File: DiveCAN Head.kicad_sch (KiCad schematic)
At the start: 50 parts, among them J1 Cell 1, J10 SOLENOID OUT, J2 Cell 2, J3 Cell 3, J4 POWER CONNECTION, Q2 DMG1012T, U13 TPS63001, U15 74LVC2G14, U16 TPS63001

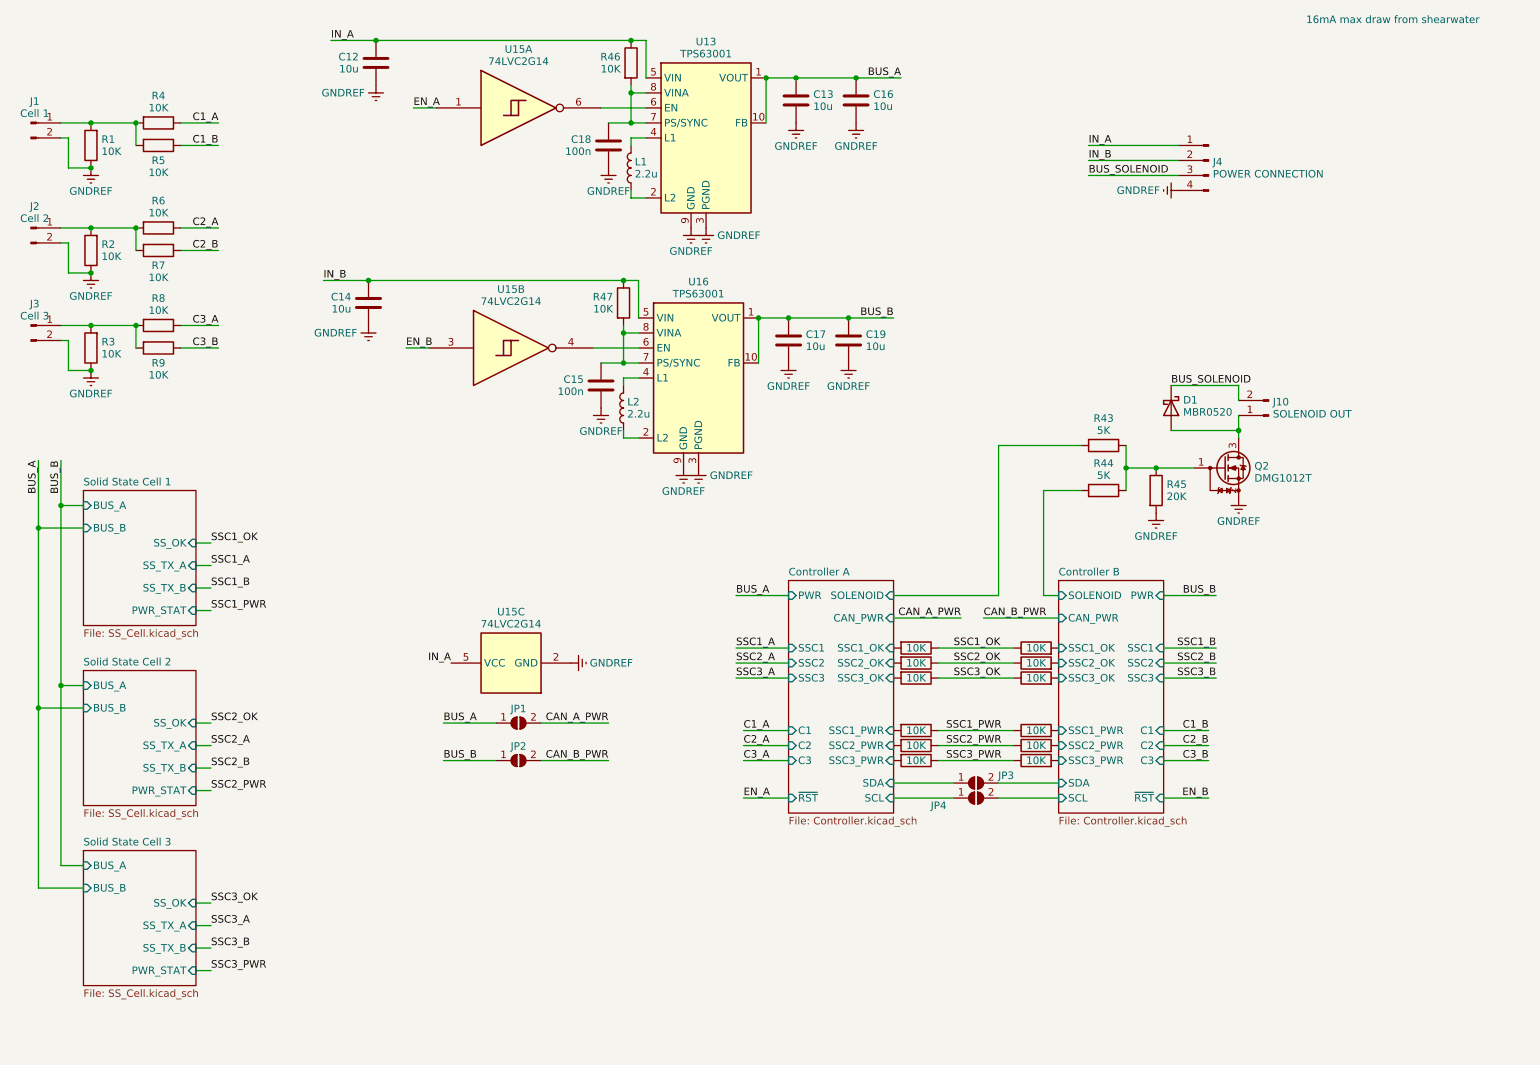
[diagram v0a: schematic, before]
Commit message: 
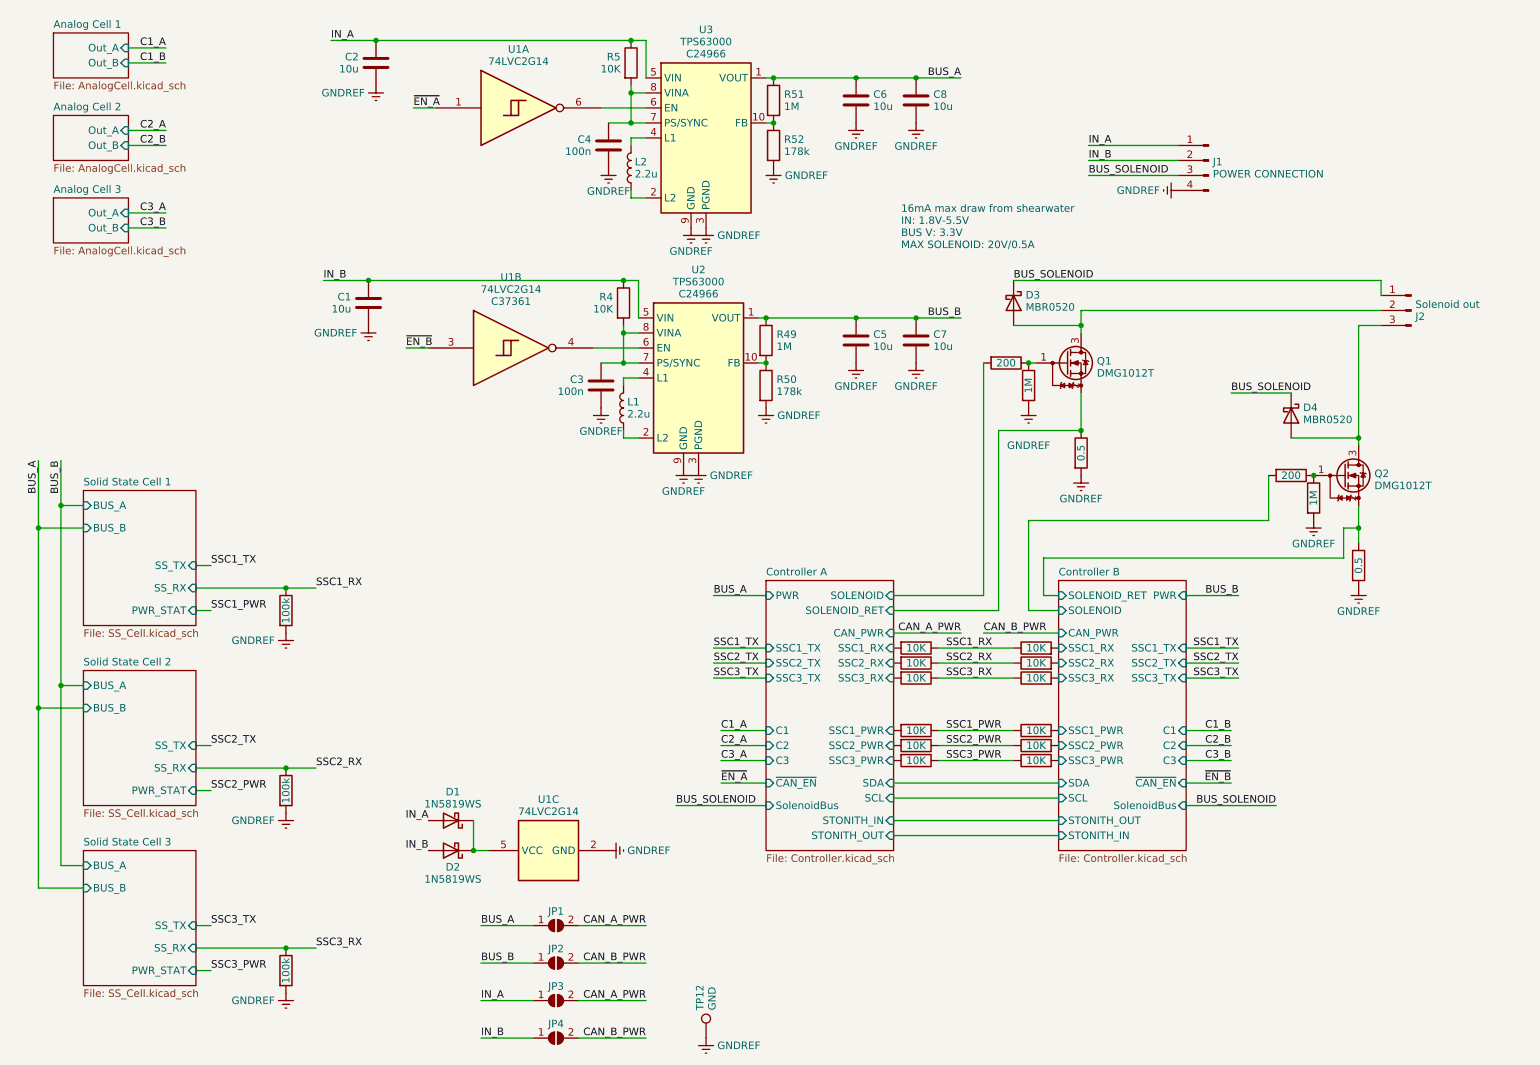
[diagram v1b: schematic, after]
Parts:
- removed J1: Cell 1, Connector_PinHeader_1.00mm:PinHeader_1x02_P1.00mm_Vertical, symbol Connector:Conn_01x02_Pin
- removed J10: SOLENOID OUT, Connector_PinHeader_1.00mm:PinHeader_1x02_P1.00mm_Vertical, symbol Connector:Conn_01x02_Pin
- removed J2: Cell 2, Connector_PinHeader_1.00mm:PinHeader_1x02_P1.00mm_Vertical, symbol Connector:Conn_01x02_Pin
- removed J3: Cell 3, Connector_PinHeader_1.00mm:PinHeader_1x02_P1.00mm_Vertical, symbol Connector:Conn_01x02_Pin
- removed R1, R2, R3, R4, R5, R6, R7, R8, R9: 10K, Resistor_SMD:R_0603_1608Metric, symbol Device:R
- removed R43, R44: 5K, Resistor_SMD:R_0603_1608Metric, symbol Device:R
- removed R45: 20K, Resistor_SMD:R_0603_1608Metric, symbol Device:R
- added D1, D2: 1N5819WS, Diode_SMD:D_SOD-323, symbol Device:D_Schottky
- added D3: MBR0520, Diode_SMD:D_SOD-123, symbol Diode:MBR0520
- added J2: Solenoid out, Connector_PinHeader_1.00mm:PinHeader_1x03_P1.00mm_Vertical, symbol Connector:Conn_01x03_Pin
- added Q1: DMG1012T, Package_TO_SOT_SMD:SOT-523, symbol Transistor_FET:DMG1012T
- added R1, R2, R3: 100k, Resistor_SMD:R_0402_1005Metric, symbol Project:R
- added R12, R21: 200, Resistor_SMD:R_0402_1005Metric, symbol Project:R
- added R13, R22, R49, R51: 1M, Resistor_SMD:R_0402_1005Metric, symbol Project:R
- added R20, R23: 0.5, Resistor_SMD:R_0402_1005Metric, symbol Project:R
- added R50, R52: 178k, Resistor_SMD:R_0402_1005Metric, symbol Project:R
- added TP12: GND, TestPoint:TestPoint_Pad_D1.0mm, symbol Connector:TestPoint
- C1: renamed from C14; MPN (none) -> C19702
- C2: renamed from C12; MPN (none) -> C19702
- C3: renamed from C15; MPN (none) -> C14663
- C4: renamed from C18; MPN (none) -> C14663
- C5: renamed from C17; MPN (none) -> C19702
- C6: renamed from C13; MPN (none) -> C19702
- C7: renamed from C19; MPN (none) -> C19702
- C8: renamed from C16; MPN (none) -> C19702
- D4: renamed from D1; MPN (none) -> C5204745
- J1: renamed from J4; now left out of the parts list
- L1: renamed from L2; footprint Inductor_SMD:L_Taiyo-Yuden_NR-30xx_HandSoldering -> Inductor_SMD:L_0805_2012Metric; MPN (none) -> C431245
- L2: renamed from L1; footprint Inductor_SMD:L_Taiyo-Yuden_NR-30xx_HandSoldering -> Inductor_SMD:L_0805_2012Metric; MPN (none) -> C431245
- Q2: JLCPCB Rotation Offset (none) -> 180; MPN (none) -> C20512
- R10: renamed from R14; footprint Resistor_SMD:R_0603_1608Metric -> Resistor_SMD:R_0402_1005Metric; symbol Device:R -> Project:R; MPN (none) -> C25744
- R11: renamed from R15; footprint Resistor_SMD:R_0603_1608Metric -> Resistor_SMD:R_0402_1005Metric; symbol Device:R -> Project:R; MPN (none) -> C25744
- R14: renamed from R16; footprint Resistor_SMD:R_0603_1608Metric -> Resistor_SMD:R_0402_1005Metric; symbol Device:R -> Project:R; MPN (none) -> C25744
- R15: renamed from R17; footprint Resistor_SMD:R_0603_1608Metric -> Resistor_SMD:R_0402_1005Metric; symbol Device:R -> Project:R; MPN (none) -> C25744
- R16: renamed from R18; footprint Resistor_SMD:R_0603_1608Metric -> Resistor_SMD:R_0402_1005Metric; symbol Device:R -> Project:R; MPN (none) -> C25744
- R17: renamed from R19; footprint Resistor_SMD:R_0603_1608Metric -> Resistor_SMD:R_0402_1005Metric; symbol Device:R -> Project:R; MPN (none) -> C25744
- R18: renamed from R20; footprint Resistor_SMD:R_0603_1608Metric -> Resistor_SMD:R_0402_1005Metric; symbol Device:R -> Project:R; MPN (none) -> C25744
- R19: renamed from R21; footprint Resistor_SMD:R_0603_1608Metric -> Resistor_SMD:R_0402_1005Metric; symbol Device:R -> Project:R; MPN (none) -> C25744
- R4: renamed from R47; footprint Resistor_SMD:R_0603_1608Metric -> Resistor_SMD:R_0402_1005Metric; symbol Device:R -> Project:R; MPN (none) -> C25744
- R5: renamed from R46; footprint Resistor_SMD:R_0603_1608Metric -> Resistor_SMD:R_0402_1005Metric; symbol Device:R -> Project:R; MPN (none) -> C25744
- R6: renamed from R10; footprint Resistor_SMD:R_0603_1608Metric -> Resistor_SMD:R_0402_1005Metric; symbol Device:R -> Project:R; MPN (none) -> C25744
- R7: renamed from R11; footprint Resistor_SMD:R_0603_1608Metric -> Resistor_SMD:R_0402_1005Metric; symbol Device:R -> Project:R; MPN (none) -> C25744
- R8: renamed from R12; footprint Resistor_SMD:R_0603_1608Metric -> Resistor_SMD:R_0402_1005Metric; symbol Device:R -> Project:R; MPN (none) -> C25744
- R9: renamed from R13; footprint Resistor_SMD:R_0603_1608Metric -> Resistor_SMD:R_0402_1005Metric; symbol Device:R -> Project:R; MPN (none) -> C25744
- U1: renamed from U15; footprint Package_SO:TSOP-6_1.65x3.05mm_P0.95mm -> Package_TO_SOT_SMD:SOT-363_SC-70-6; JLCPCB Rotation Offset (none) -> 180; MPN (none) -> C37361
- U1: renamed from U15; footprint Package_SO:TSOP-6_1.65x3.05mm_P0.95mm -> Package_TO_SOT_SMD:SOT-363_SC-70-6; symbol 74xGxx:74LVC2G14 -> Project:74LVC2G14; JLCPCB Rotation Offset (none) -> 180; MPN (none) -> C37361
- U2: renamed from U16; value TPS63001 -> TPS63000; footprint Package_SON:Texas_DRC0010J_ThermalVias -> Package_SON:Texas_DRC0010J; symbol Regulator_Switching:TPS63001 -> Project:TPS63001; MPN (none) -> C24966
- U3: renamed from U13; value TPS63001 -> TPS63000; footprint Package_SON:Texas_DRC0010J_ThermalVias -> Package_SON:Texas_DRC0010J; symbol Regulator_Switching:TPS63001 -> Project:TPS63001; MPN (none) -> C24966
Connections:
- net Controller B/SCL is gone; now on net CAN_B_PWR: JP4.2 (B)
- net Controller B/SDA is gone; now on net CAN_A_PWR: JP3.2 (B)
- net BUS_A: now also R51.1; no longer U3.10 (FB)
- net BUS_B: now also R49.1; no longer U2.10 (FB)
- net BUS_SOLENOID: now also D3.1 (K), J2.1 (Pin_1)
- net Controller A/SCL: no longer JP4.1 (A)
- net Controller A/SDA: no longer JP3.1 (A)
- net Controller A/SOLENOID: now also R12.2
- net Controller B/SOLENOID: now also R21.2
- net GNDREF: now also R1.2, R13.2, R2.2, R20.2, R22.2, R23.2, R3.2, R50.2, R52.2, TP12.1; no longer Q2.2 (S)
- net IN_A: now also JP3.1 (A), D1.2 (A); no longer U1.5 (VCC)
- net IN_B: now also JP4.1 (A), D2.2 (A)
- net at Q2.1 (G): now also R21.1, R22.1
- net at D4.2 (A), Q2.3 (D): now also J2.3 (Pin_3)
- net Controller A/SSC1_OK renamed Controller A/SSC1_RX
- net Controller A/SSC2_OK renamed Controller A/SSC2_RX
- net Controller A/SSC3_OK renamed Controller A/SSC3_RX
- net Controller B/SSC1_OK renamed Controller B/SSC1_RX
- net Controller B/SSC2_OK renamed Controller B/SSC2_RX
- net Controller B/SSC3_OK renamed Controller B/SSC3_RX
- net EN_A renamed ~{EN_A}
- net EN_B renamed ~{EN_B}
- net SSC1_OK renamed SSC1_RX
- net SSC1_RX: now also R1.1
- net SSC2_OK renamed SSC2_RX
- net SSC2_RX: now also R2.1
- net SSC3_OK renamed SSC3_RX
- net SSC3_RX: now also R3.1
- new net: D3.2 (A), J2.2 (Pin_2), Q1.3 (D)
- new net: Q1.1 (G), R12.1, R13.1
- new net: D1.1 (K), D2.1 (K), U1.5 (VCC)
- new net: R49.2, R50.1, U2.10 (FB)
- new net: R51.2, R52.1, U3.10 (FB)
- new net Controller A/SOLENOID_RET: Q1.2 (S), R20.1
- new net Controller B/SOLENOID_RET: Q2.2 (S), R23.1
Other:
- added sheet Analog Cell 1 (AnalogCell.kicad_sch)
- added sheet Analog Cell 2 (AnalogCell.kicad_sch)
- added sheet Analog Cell 3 (AnalogCell.kicad_sch)
- sheet Controller A ports: added SOLENOID_RET, SSC1_RX, SSC1_TX, SSC2_RX, SSC2_TX, SSC3_RX, SSC3_TX, STONITH_IN, STONITH_OUT, SolenoidBus, ~{CAN_EN}; removed SSC1, SSC1_OK, SSC2, SSC2_OK, SSC3, SSC3_OK, ~{RST}
- sheet Controller B ports: added SOLENOID_RET, SSC1_RX, SSC1_TX, SSC2_RX, SSC2_TX, SSC3_RX, SSC3_TX, STONITH_IN, STONITH_OUT, SolenoidBus, ~{CAN_EN}; removed SSC1, SSC1_OK, SSC2, SSC2_OK, SSC3, SSC3_OK, ~{RST}
- sheet Solid State Cell 1 ports: added SS_RX, SS_TX; removed SS_OK, SS_TX_A, SS_TX_B
- sheet Solid State Cell 2 ports: added SS_RX, SS_TX; removed SS_OK, SS_TX_A, SS_TX_B
- sheet Solid State Cell 3 ports: added SS_RX, SS_TX; removed SS_OK, SS_TX_A, SS_TX_B
- note added: "16mA max draw from shearwater IN: 1.8V-5.5V BUS V: 3.3V MAX SOLENOID: 20V/0.5A"
- note removed: "16mA max draw from shearwater"
- moved on the sheet: C5, C6, C7, C8, D4, JP1, JP2, Q2, U1C
